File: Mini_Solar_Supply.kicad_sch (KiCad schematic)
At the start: 16 parts, among them J1 Conn_01x02_Pin, J2 Conn_01x02_Pin, J3 Conn_01x02_Pin, J4 Conn_01x02_Pin, Q1 2N7002, U1 AP3015AKTR-G1

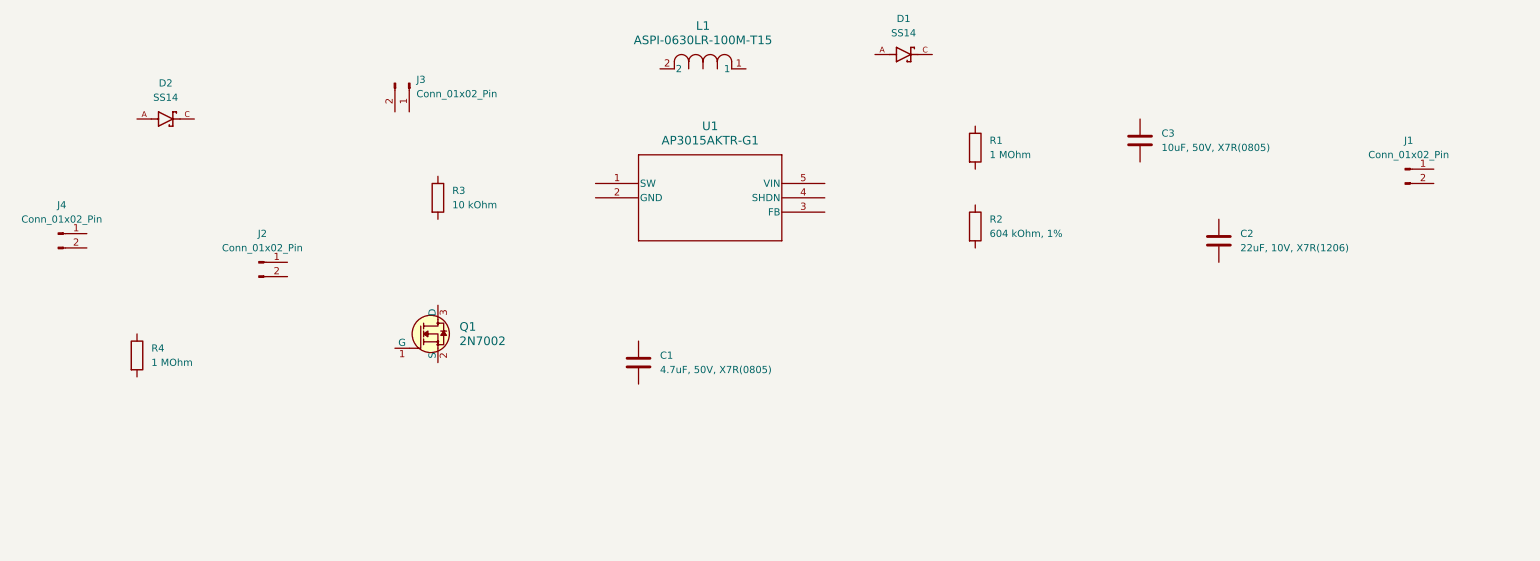
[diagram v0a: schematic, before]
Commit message: changed the AP3015AKTR-G1 to alighn the pins and connected all the components in the schematic circuit
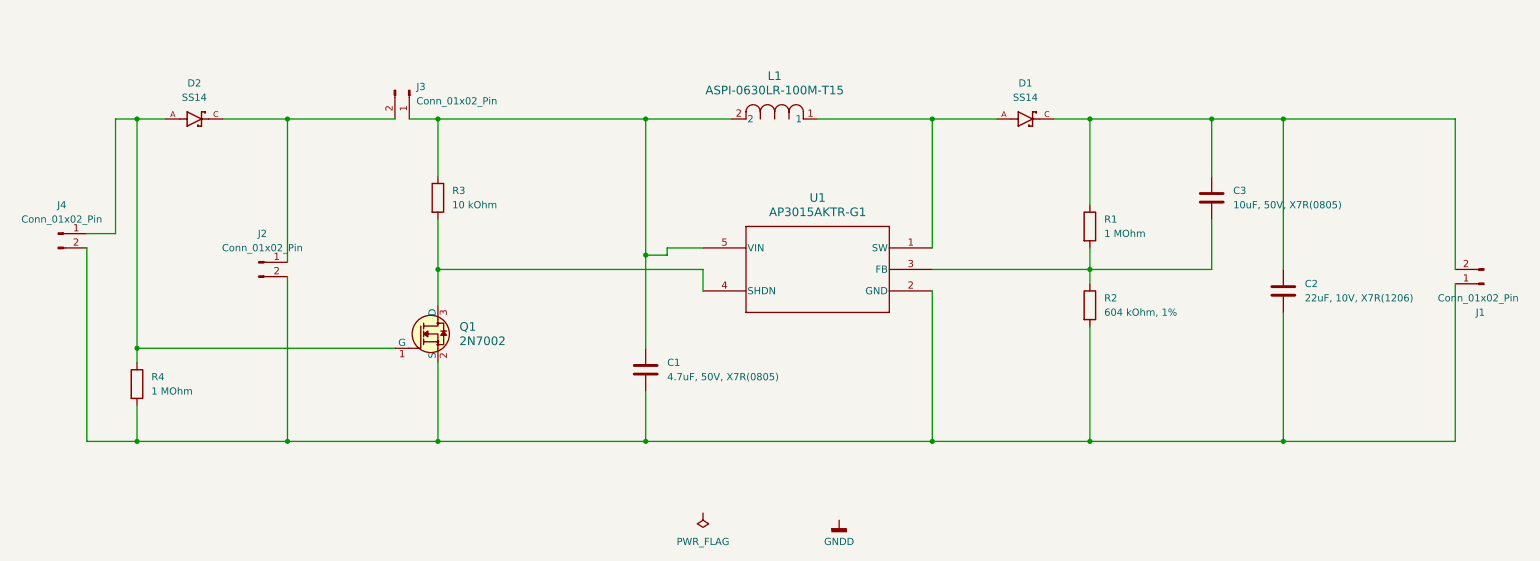
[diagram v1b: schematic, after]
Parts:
- U1: footprint AP3015AKTR-G1:SOT23-5_1P55X2P9_DIO-M -> SOT23-5_1P55X2P9_DIO
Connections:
- net at J3.1 (Pin_1): now also C1.1, L1.2, R3.1, U1.5 (VIN)
- net at J3.2 (Pin_2): now also D2.C, J2.1 (Pin_1)
- net at J4.1 (Pin_1): now also D2.A, Q1.1 (G), R4.1
- net at J4.2 (Pin_2): now also C1.2, C2.2, J1.1 (Pin_1), J2.2 (Pin_2), Q1.2 (S), R2.2, R4.2, U1.2 (GND)
- net at C3.1: now also C2.1, D1.C, J1.2 (Pin_2), R1.1
- net at C3.2: now also R1.2, R2.1, U1.3 (FB)
- net at R3.2: now also Q1.3 (D), U1.4 (SHDN)
- net at D1.A: now also L1.1, U1.1 (SW)
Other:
- moved on the sheet: C1, C2, C3, D1, D2, J1, J3, L1, R1, R2, R4, U1

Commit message: fixed errors and performed CRC check
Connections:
- net GNDD: now also C1.2, C2.2, J1.1 (Pin_1), J2.2 (Pin_2), J4.2 (Pin_2), Q1.2 (S), R2.2, R4.2, U1.2 (GND)
- net BAT_P: now reaches D2.C, J2.1 (Pin_1), J3.2 (Pin_2)
- net Solar_P+: now reaches D2.A, J4.1 (Pin_1), Q1.1 (G), R4.1
- net OUT_P: now reaches C2.1, C3.1, D1.C, J1.2 (Pin_2), R1.1
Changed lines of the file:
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@@
+	)
+	(junction
+		(at 35.56 138.43)
+		(diameter 0)
+		(color 0 0 0 0)
+	)
+	(junction
+		(at 88.9 81.28)
+		(diameter 0)
+		(color 0 0 0 0)
+	)
+	(junction
+		(at 238.76 81.28)
+		(diameter 0)
+		(color 0 0 0 0)
+	)
+	(junction
+		(at 35.56 121.92)
+		(diameter 0)
+		(color 0 0 0 0)
+	)
+	(junction
+		(at 153.67 138.43)
+		(diameter 0)
+		(color 0 0 0 0)
+	)
+	(junction
+		(at 135.89 138.43)
+		(diameter 0)
+		(color 0 0 0 0)
+	)
+	(junction
+		(at 204.47 107.95)
+		(diameter 0)
+		(color 0 0 0 0)
+	)
+	(junction
+		(at 226.06 81.28)
+		(diameter 0)
+		(color 0 0 0 0)
+	)
+	(junction
+		(at 125.73 81.28)
+		(diameter 0)
+		(color 0 0 0 0)
+	)
+	(junction
+		(at 125.73 105.41)
+		(diameter 0)
+		(color 0 0 0 0)
+	)
+	(junction
+		(at 88.9 107.95)
+		(diameter 0)
+		(color 0 0 0 0)
+	)
+	(junction
+		(at 204.47 138.43)
+		(diameter 0)
+		(color 0 0 0 0)
+	)
+	(junction
+		(at 62.23 138.43)
+		(diameter 0)
+		(color 0 0 0 0)
+	)
+	(junction
+		(at 176.53 81.28)
+		(diameter 0)
+		(color 0 0 0 0)
+	)
+	(junction
+		(at 35.56 81.28)
+		(diameter 0)
+		(color 0 0 0 0)
+	)
+	(junction
+		(at 182.88 138.43)
+		(diameter 0)
+		(color 0 0 0 0)
 	)
 	(junction
@@
 	)
 	(junction
-		(at 35.56 138.43)
-		(diameter 0)
-		(color 0 0 0 0)
-	)
-	(junction
-		(at 88.9 81.28)
-		(diameter 0)
-		(color 0 0 0 0)
-	)
-	(junction
-		(at 176.53 138.43)
-		(diameter 0)
-		(color 0 0 0 0)
-	)
-	(junction
-		(at 238.76 81.28)
-		(diameter 0)
-		(color 0 0 0 0)
-	)
-	(junction
-		(at 35.56 121.92)
-		(diameter 0)
-		(color 0 0 0 0)
-	)
-	(junction
-		(at 204.47 107.95)
-		(diameter 0)
-		(color 0 0 0 0)
-	)
-	(junction
-		(at 226.06 81.28)
-		(diameter 0)
-		(color 0 0 0 0)
-	)
-	(junction
-		(at 125.73 81.28)
-		(diameter 0)
-		(color 0 0 0 0)
-	)
-	(junction
-		(at 125.73 105.41)
-		(diameter 0)
-		(color 0 0 0 0)
-	)
-	(junction
-		(at 88.9 107.95)
-		(diameter 0)
-		(color 0 0 0 0)
-	)
-	(junction
-		(at 204.47 138.43)
-		(diameter 0)
-		(color 0 0 0 0)
-	)
-	(junction
-		(at 62.23 138.43)
-		(diameter 0)
-		(color 0 0 0 0)
-	)
-	(junction
-		(at 176.53 81.28)
-		(diameter 0)
-		(color 0 0 0 0)
-	)
-	(junction
-		(at 35.56 81.28)
-		(diameter 0)
-		(color 0 0 0 0)
-	)
-	(junction
 		(at 204.47 81.28)
 		(diameter 0)
@@
 	(wire
 		(pts
+			(xy 135.89 138.43) (xy 125.73 138.43)
+		)
+		(stroke
+			(width 0)
+			(type default)
+		)
+	)
+	(wire
+		(pts
 			(xy 125.73 105.41) (xy 125.73 121.92)
 		)
@@
 	(wire
 		(pts
-			(xy 204.47 138.43) (xy 176.53 138.43)
-		)
-		(stroke
-			(width 0)
-			(type default)
-		)
-	)
-	(wire
-		(pts
 			(xy 125.73 81.28) (xy 140.97 81.28)
 		)
@@
 	(wire
 		(pts
-			(xy 176.53 111.76) (xy 176.53 138.43)
-		)
-		(stroke
-			(width 0)
-			(type default)
-		)
-	)
-	(wire
-		(pts
 			(xy 204.47 118.11) (xy 204.47 138.43)
 		)
@@
 	(wire
 		(pts
+			(xy 182.88 111.76) (xy 182.88 138.43)
+		)
+		(stroke
+			(width 0)
+			(type default)
+		)
+	)
+	(wire
+		(pts
 			(xy 35.56 138.43) (xy 62.23 138.43)
 		)
@@
 	(wire
 		(pts
+			(xy 88.9 124.46) (xy 88.9 138.43)
+		)
+		(stroke
+			(width 0)
+			(type default)
+		)
+	)
+	(wire
+		(pts
+			(xy 135.89 138.43) (xy 135.89 147.32)
+		)
+		(stroke
+			(width 0)
+			(type default)
+		)
+	)
+	(wire
+		(pts
 			(xy 88.9 99.06) (xy 88.9 107.95)
 		)
@@
 	(wire
 		(pts
+			(xy 176.53 111.76) (xy 182.88 111.76)
+		)
+		(stroke
+			(width 0)
+			(type default)
+		)
+	)
+	(wire
+		(pts
 			(xy 35.56 121.92) (xy 81.28 121.92)
 		)
@@
 	(wire
 		(pts
+			(xy 88.9 138.43) (xy 125.73 138.43)
+		)
+		(stroke
+			(width 0)
+			(type default)
+		)
+	)
+	(wire
+		(pts
 			(xy 204.47 81.28) (xy 198.12 81.28)
 		)
@@
 	(wire
 		(pts
-			(xy 176.53 138.43) (xy 125.73 138.43)
+			(xy 153.67 138.43) (xy 182.88 138.43)
+		)
+		(stroke
+			(width 0)
+			(type default)
+		)
+	)
+	(wire
+		(pts
+			(xy 153.67 138.43) (xy 153.67 147.32)
 		)
 		(stroke
@@
 	(wire
 		(pts
-			(xy 125.73 138.43) (xy 88.9 138.43)
+			(xy 153.67 138.43) (xy 135.89 138.43)
 		)
 		(stroke
@@
 	(wire
 		(pts
+			(xy 182.88 138.43) (xy 204.47 138.43)
+		)
+		(stroke
+			(width 0)
+			(type default)
+		)
+	)
+	(wire
+		(pts
 			(xy 226.06 99.06) (xy 226.06 107.95)
 		)
@@
 	(wire
 		(pts
-			(xy 88.9 138.43) (xy 88.9 124.46)
-		)
-		(stroke
-			(width 0)
-			(type default)
-		)
-	)
-	(wire
-		(pts
 			(xy 238.76 81.28) (xy 226.06 81.28)
 		)
@@
 			(width 0)
 			(type default)
+		)
+	)
+	(label "Solar_P+"
+		(at 31.75 81.28 180)
+		(effects
+			(font
+				(size 1.27 1.27)
+			)
+			(justify right bottom)
+		)
+	)
+	(label "OUT_P"
+		(at 269.24 81.28 0)
+		(effects
+			(font
+				(size 1.27 1.27)
+			)
+			(justify left bottom)
+		)
+	)
+	(label "BAT_P"
+		(at 62.23 95.25 0)
+		(effects
+			(font
+				(size 1.27 1.27)
+			)
+			(justify left bottom)
 		)
 	)
@@
 	(symbol
 		(lib_id "power:PWR_FLAG")
-		(at 135.89 151.13 180)
+		(at 135.89 147.32 180)
 		(unit 1)
 		(exclude_from_sim no)
@@
 		(fields_autoplaced yes)
 		(property "Reference" "#FLG01"
-			(at 135.89 153.035 0)
+			(at 135.89 149.225 0)
 			(effects
 				(font
@@
 		)
 		(property "Value" "PWR_FLAG"
-			(at 135.89 156.21 0)
+			(at 135.89 152.4 0)
 			(effects
 				(font
@@
 		)
 		(property "Footprint" ""
-			(at 135.89 151.13 0)
+			(at 135.89 147.32 0)
 			(effects
 				(font
@@
 		)
 		(property "Datasheet" "~"
-			(at 135.89 151.13 0)
+			(at 135.89 147.32 0)
 			(effects
 				(font
@@
 		)
 		(property "Description" "Special symbol for telling ERC where power comes from"
-			(at 135.89 151.13 0)
+			(at 135.89 147.32 0)
 			(effects
 				(font
@@
 	(symbol
 		(lib_id "power:GNDD")
-		(at 160.02 152.4 0)
+		(at 153.67 147.32 0)
 		(unit 1)
 		(exclude_from_sim no)
@@
 		(fields_autoplaced yes)
 		(property "Reference" "#PWR01"
-			(at 160.02 158.75 0)
+			(at 153.67 153.67 0)
 			(effects
 				(font
@@
 		)
 		(property "Value" "GNDD"
-			(at 160.02 156.21 0)
+			(at 153.67 151.13 0)
 			(effects
 				(font
@@
 		)
 		(property "Footprint" ""
-			(at 160.02 152.4 0)
+			(at 153.67 147.32 0)
 			(effects
 				(font
@@
 		)
 		(property "Datasheet" ""
-			(at 160.02 152.4 0)
+			(at 153.67 147.32 0)
 			(effects
 				(font
@@
 		)
 		(property "Description" "Power symbol creates a global label with name \"GNDD\" , digital ground"
-			(at 160.02 152.4 0)
-			(effects
-				(font
+			(at 153.67 147.32 0)
+			(effects
+				(font
